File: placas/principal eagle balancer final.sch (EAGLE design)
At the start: 12 parts, among them X1 RJ45

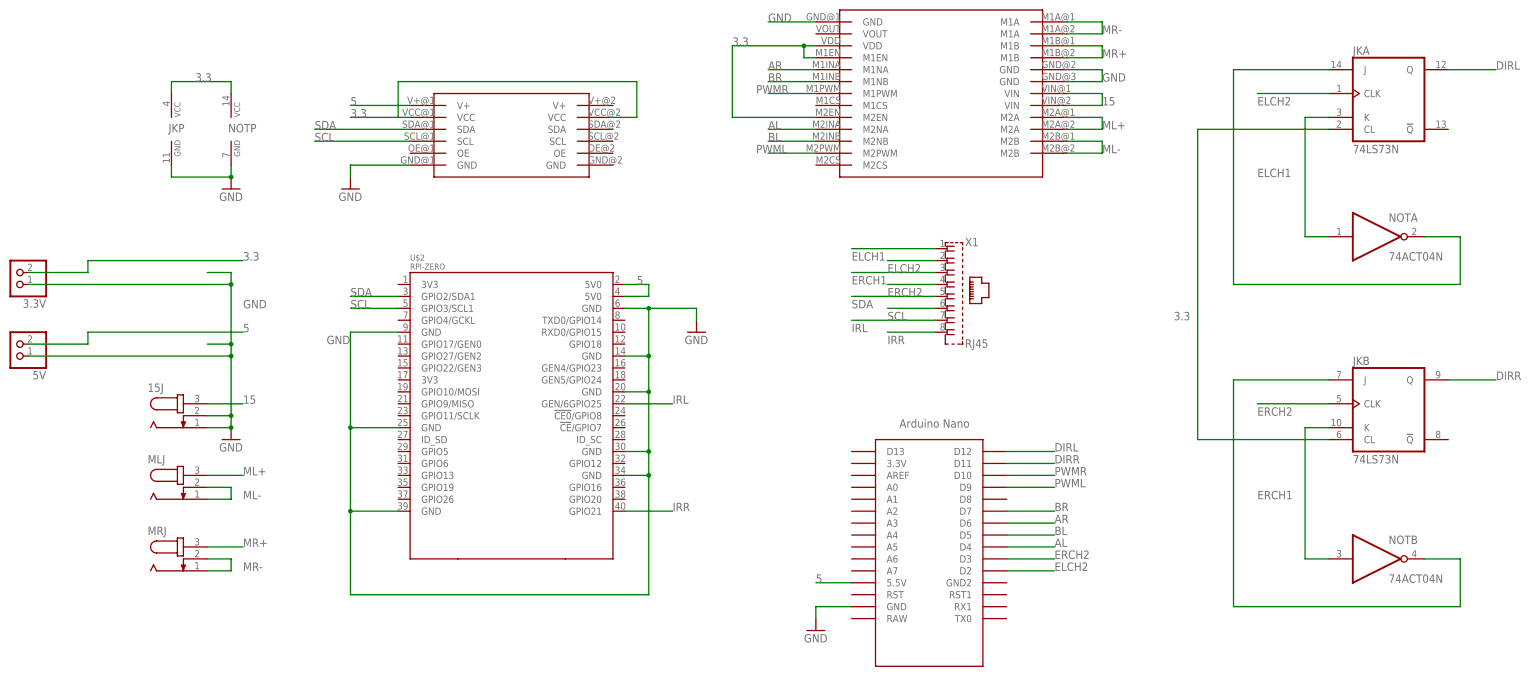
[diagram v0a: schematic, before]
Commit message: Versão final placa principal
Corrigidas as trilhas que levan a tensão de 3.3 a 5V nos CI 7473 e 7404
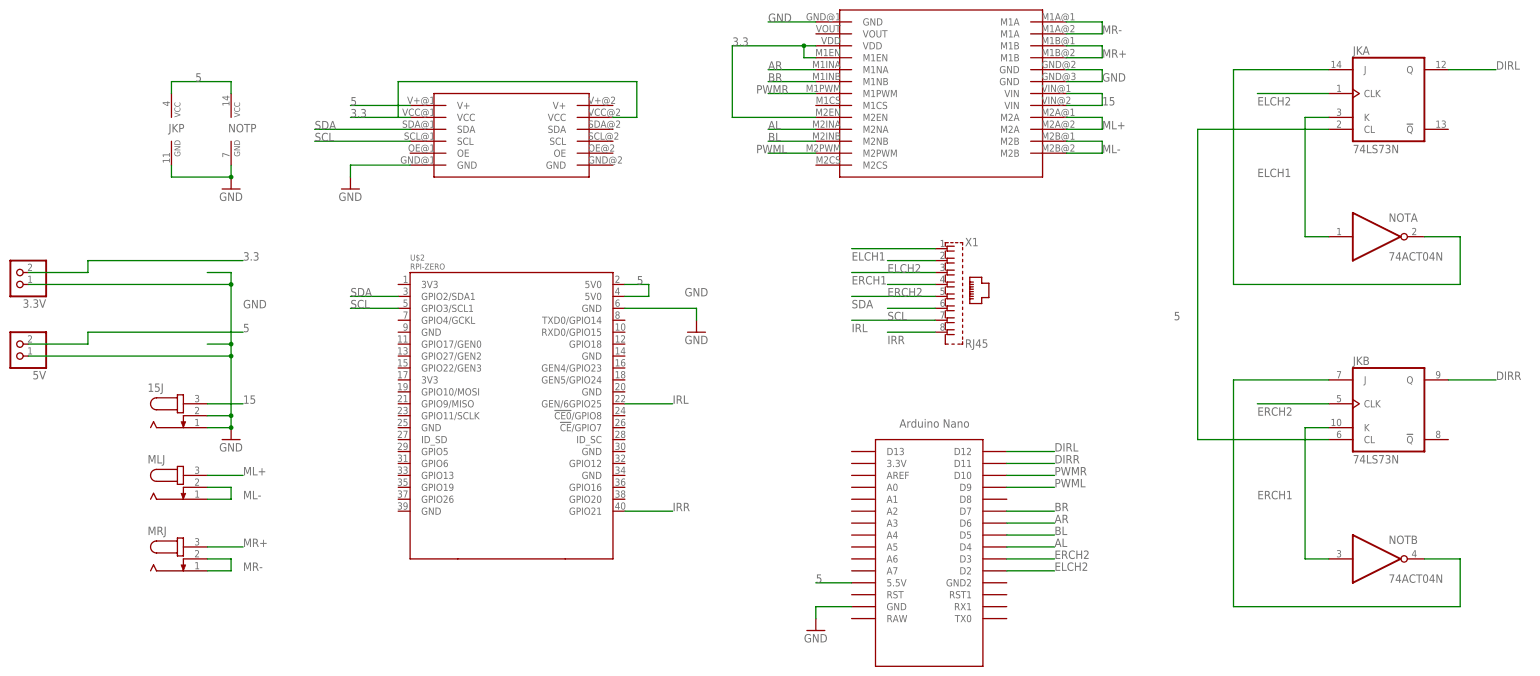
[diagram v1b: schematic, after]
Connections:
- net 3.3: no longer JKA.CL, JKB.CL, JKP.VCC, NOTP.VCC
- net 5: now also JKA.CL, JKB.CL, JKP.VCC, NOTP.VCC
- net GND: no longer U$2.GND@1, U$2.GND@2, U$2.GND@3, U$2.GND@4, U$2.GND@5, U$2.GND@6, U$2.GND@7
